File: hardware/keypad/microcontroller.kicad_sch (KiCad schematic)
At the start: 0 parts

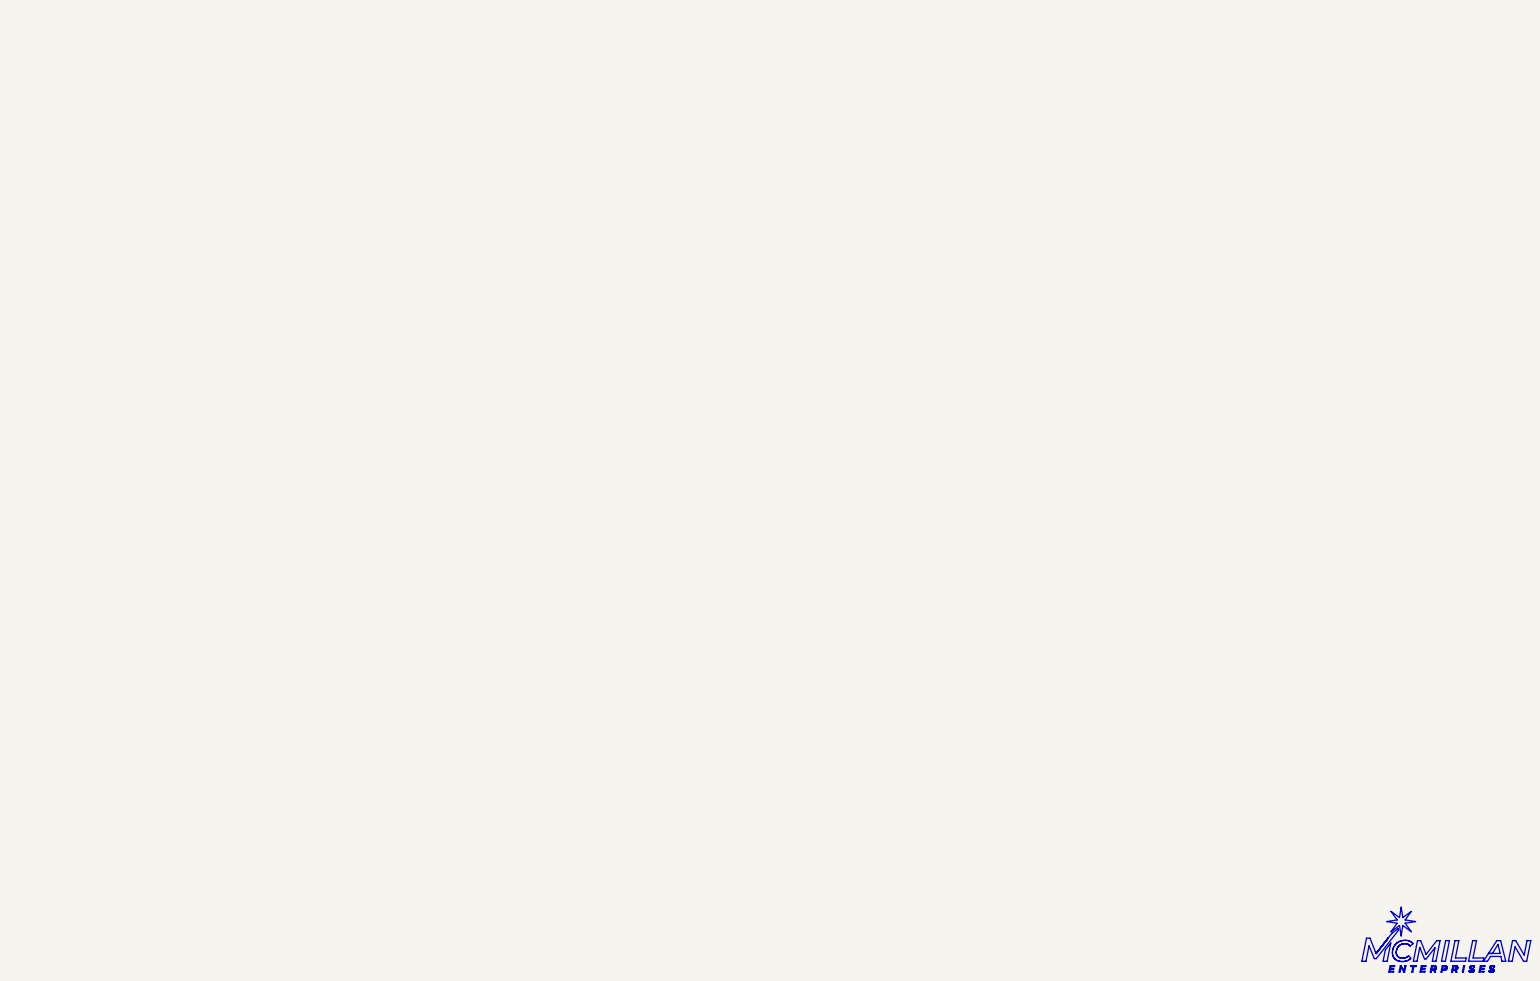
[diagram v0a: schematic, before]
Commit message: Revision X2!
New and improved revision of the keypad! I fixed issues with the repeater and remote SBC power switch circuit (hopefully🤞). I also integrated the Arduino Nano onto the board (ATMEGA328).
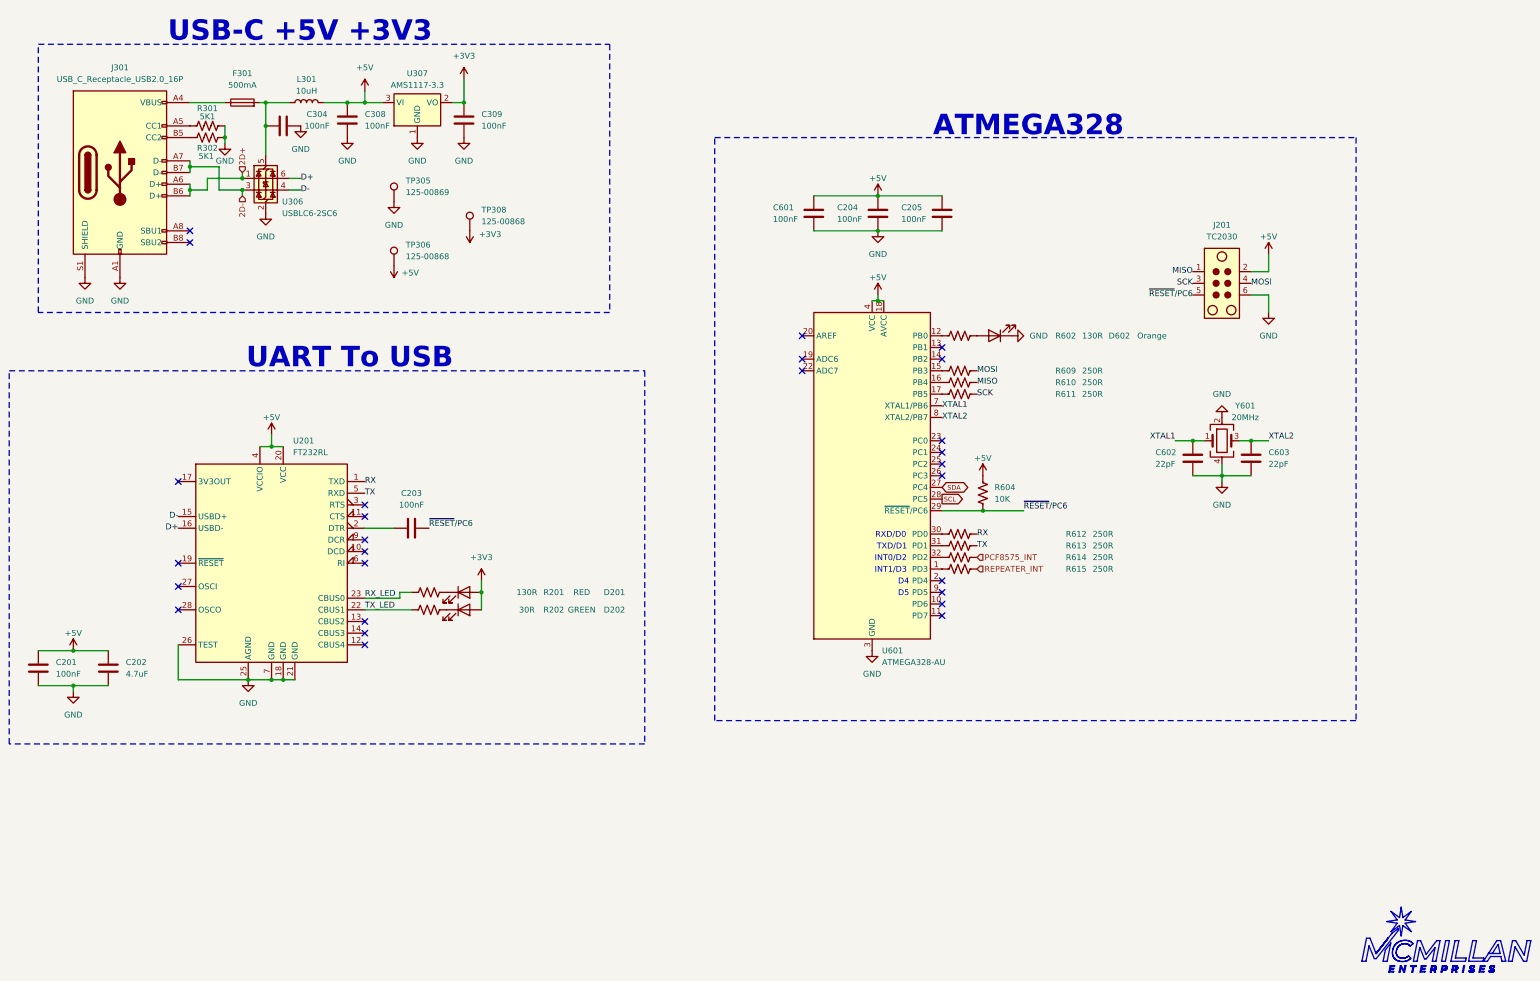
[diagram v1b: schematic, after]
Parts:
- added C201, C203, C204, C205, C304, C308, C309, C601: 100nF, Capacitor_SMD:C_0805_2012Metric, symbol Device:C
- added C202: 4.7uF, Capacitor_SMD:C_0805_2012Metric, symbol Device:C
- added C602, C603: 22pF, Capacitor_SMD:C_0805_2012Metric, symbol Device:C
- added D201: RED, LED_SMD:LED_0805_2012Metric, symbol Device:LED
- added D202: GREEN, LED_SMD:LED_0805_2012Metric, symbol Device:LED
- added D602: Orange, LED_SMD:LED_0805_2012Metric, symbol Device:LED
- added F301: 500mA, Fuse:Fuse_0805_2012Metric, symbol Device:Fuse
- added J201: TC2030, Connector:Tag-Connect_TC2030-IDC-NL_2x03_P1.27mm_Vertical, symbol Connector:TC2030
- added J301: USB_C_Receptacle_USB2.0_16P, Connector_USB:USB_C_Receptacle_G-Switch_GT-USB-7010ASV, symbol Connector:USB_C_Receptacle_USB2.0_16P
- added L301: 10uH, Inductor_SMD:L_0805_2012Metric, symbol Device:L
- added R201, R602: 130R, Resistor_SMD:R_0805_2012Metric, symbol Device:R_US
- added R202: 30R, Resistor_SMD:R_0805_2012Metric, symbol Device:R_US
- added R301, R302: 5K1, Resistor_SMD:R_0805_2012Metric, symbol Device:R_US
- added R604: 10K, Resistor_SMD:R_0805_2012Metric, symbol Device:R_US
- added R609, R610, R611, R612, R613, R614, R615: 250R, Resistor_SMD:R_0805_2012Metric, symbol Device:R_US
- added TP305: 125-00869, TestPoint:TestPoint_Keystone_5000-5004_Miniature, symbol Connector:TestPoint
- added TP306, TP308: 125-00868, TestPoint:TestPoint_Keystone_5000-5004_Miniature, symbol Connector:TestPoint
- added U201: FT232RL, Package_SO:SSOP-28_5.3x10.2mm_P0.65mm, symbol Interface_USB:FT232RL
- added U306: USBLC6-2SC6, Package_TO_SOT_SMD:SOT-23-6, symbol Power_Protection:USBLC6-2SC6
- added U307: AMS1117-3.3, Package_TO_SOT_SMD:SOT-223-3_TabPin2, symbol Regulator_Linear:AMS1117-3.3
- added U601: ATMEGA328-AU, Package_QFP:TQFP-32_7x7mm_P0.8mm, symbol MCU_Microchip_ATmega:ATmega328-A
- added Y601: 20MHz, Crystal:Crystal_SMD_3225-4Pin_3.2x2.5mm, symbol Device:Crystal_GND24
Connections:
- new net: R615.1, U601.1 (PD3)
- new net: R612.1, U601.30 (PD0)
- new net: C304.2, F301.2, L301.1, U306.5 (VBUS)
- new net: D602.2 (A), R602.2
- new net: J301.B5 (CC2), R302.2
- new net: D202.1 (K), R202.1
- new net: D201.1 (K), R201.1
- new net: C203.1, U201.2 (DTR)
- new net: R614.1, U601.32 (PD2)
- new net: R610.1, U601.16 (PB4)
- new net: R611.1, U601.17 (PB5)
- new net: R613.1, U601.31 (PD1)
- new net: F301.1, J301.A4 (VBUS), J301.A9 (VBUS), J301.B4 (VBUS), J301.B9 (VBUS)
- new net: J301.A5 (CC1), R301.2
- new net: R602.1, U601.12 (PB0)
- new net: R609.1, U601.15 (PB3)
- new net +3V3: C309.1, D201.2 (A), D202.2 (A), TP308.1, U307.2 (VO)
- new net +5V: C201.1, C202.1, C204.1, C205.1, C308.1, C601.1, J201.2, L301.2, R604.1, TP306.1, U201.20 (VCC), U201.4 (VCCIO), U307.3 (VI), U601.18 (AVCC), U601.4 (VCC), U601.6 (VCC)
- new net 2D+: J301.A6 (D+), J301.B6 (D+), U306.1 (I/O1)
- new net 2D-: J301.A7 (D-), J301.B7 (D-), U306.3 (I/O2)
- new net D+: U201.16 (USBD-), U306.6 (I/O1)
- new net D-: U201.15 (USBD+), U306.4 (I/O2)
- new net GND: C201.2, C202.2, C204.2, C205.2, C304.1, C308.2, C309.2, C601.2, C602.2, C603.2, D602.1 (K), J201.6, J301.A1 (GND), J301.A12 (GND), J301.B1 (GND), J301.B12 (GND), J301.S1 (SHIELD), R301.1, R302.1, TP305.1, U201.18 (GND), U201.21 (GND), U201.25 (AGND), U201.26 (TEST), U201.7 (GND), U306.2 (GND), U307.1 (GND), U601.21 (GND), U601.3 (GND), U601.5 (GND), Y601.2, Y601.4
- new net MISO: J201.1, R610.2
- new net MOSI: J201.4, R609.2
- new net PCF8575_INT: R614.2
- new net REPEATER_INT: R615.2
- new net RX: R612.2, U201.1 (TXD)
- new net RX_LED: R201.2, U201.23 (CBUS0)
- new net SCK: J201.3, R611.2
- new net SCL: U601.28 (PC5)
- new net SDA: U601.27 (PC4)
- new net TX: R613.2, U201.5 (RXD)
- new net TX_LED: R202.2, U201.22 (CBUS1)
- new net XTAL1: C602.1, U601.7 (XTAL1/PB6), Y601.1
- new net XTAL2: C603.1, U601.8 (XTAL2/PB7), Y601.3
- new net ~{RESET}/PC6: C203.2, J201.5, R604.2, U601.29 (~{RESET}/PC6)
- no-connect marks 0 -> 27
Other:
- note added: "ATMEGA328"
- note added: "D4"
- note added: "D5"
- note added: "INT0/D2"
- note added: "INT1/D3"
- note added: "RXD/D0"
- note added: "TXD/D1"
- note added: "UART To USB"
- note added: "USB-C +5V +3V3"
